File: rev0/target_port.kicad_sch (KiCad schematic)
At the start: 12 parts, among them IC1 ECP5-BGA256, U9 USB3343-CP

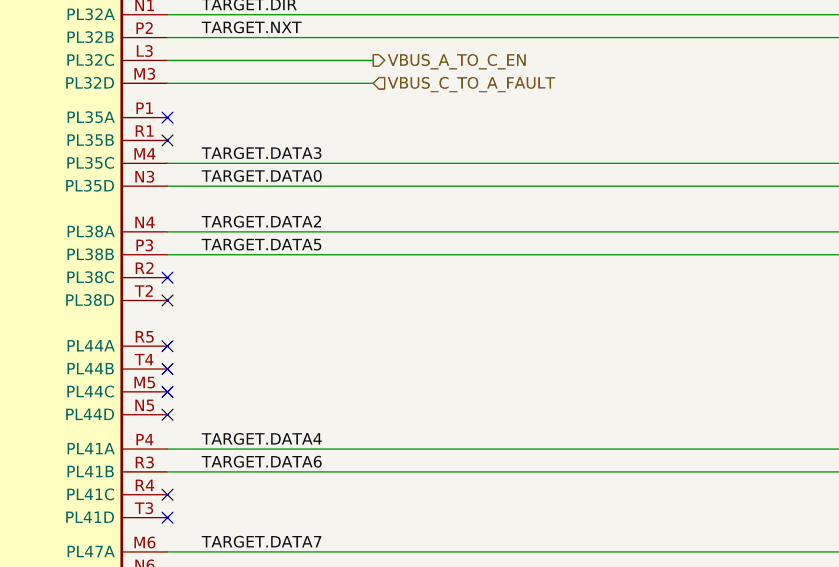
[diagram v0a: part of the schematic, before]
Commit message: hardware: add Target D+/D- full-speed monitor
allows FPGA to monitor low-speed or full-speed USB directly (instead of
or in addition to the high-speed PHY)
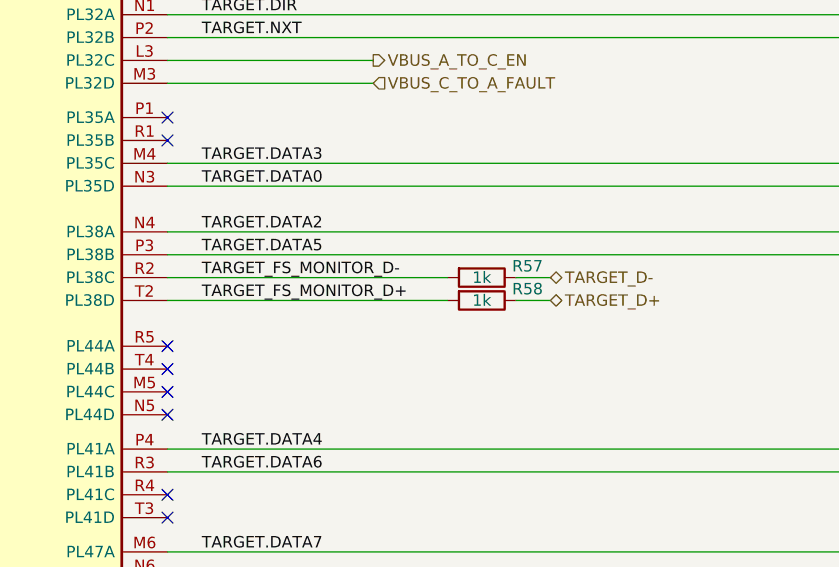
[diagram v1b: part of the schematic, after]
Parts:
- added R57, R58: 1k, Resistor_SMD:R_0402_1005Metric, symbol Device:R
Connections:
- net TARGET_D+: now also R58.1
- net TARGET_D-: now also R57.1
- net TARGET_FS_MONITOR_D-: now reaches IC1.R2 (PL38C)
- net TARGET_FS_MONITOR_D-: now also R57.2
- net TARGET_FS_MONITOR_D+: now reaches IC1.T2 (PL38D)
- net TARGET_FS_MONITOR_D+: now also R58.2
- no-connect marks 12 -> 10
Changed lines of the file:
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@@
   (junction (at 123.19 67.31) (diameter 0) (color 0 0 0 0)
   )
-  (no_connect (at 59.69 105.41))
-  (no_connect (at 59.69 107.95))
   (no_connect (at 59.69 118.11))
   (no_connect (at 59.69 115.57))
@@
     (stroke (width 0) (type default) (color 0 0 0 0))
   )
+  (wire (pts (xy 59.69 105.41) (xy 90.805 105.41))
+    (stroke (width 0) (type default) (color 0 0 0 0))
+  )
   (wire (pts (xy 59.69 72.39) (xy 137.16 72.39))
     (stroke (width 0) (type default) (color 0 0 0 0))
@@
     (stroke (width 0) (type default) (color 0 0 0 0))
   )
+  (wire (pts (xy 102.235 105.41) (xy 98.425 105.41))
+    (stroke (width 0) (type default) (color 0 0 0 0))
+  )
   (wire (pts (xy 231.14 63.5) (xy 226.06 63.5))
     (stroke (width 0) (type default) (color 0 0 0 0))
@@
     (stroke (width 0) (type default) (color 0 0 0 0))
   )
+  (wire (pts (xy 102.235 107.95) (xy 98.425 107.95))
+    (stroke (width 0) (type default) (color 0 0 0 0))
+  )
   (wire (pts (xy 165.1 90.17) (xy 190.5 90.17))
     (stroke (width 0) (type default) (color 0 0 0 0))
@@
     (stroke (width 0) (type default) (color 0 0 0 0))
   )
+  (wire (pts (xy 59.69 107.95) (xy 90.805 107.95))
+    (stroke (width 0) (type default) (color 0 0 0 0))
+  )
   (wire (pts (xy 41.91 31.75) (xy 41.91 34.29))
     (stroke (width 0) (type default) (color 0 0 0 0))
@@
     (effects (font (size 1.27 1.27)) (justify left bottom))
   )
+  (label "TARGET_FS_MONITOR_D-" (at 63.5 105.41 0)
+    (effects (font (size 1.27 1.27)) (justify left bottom))
+  )
   (label "TARGET.STP" (at 63.5 60.96 0)
     (effects (font (size 1.27 1.27)) (justify left bottom))
@@
   )
   (label "TARGET.NXT" (at 63.5 78.74 0)
+    (effects (font (size 1.27 1.27)) (justify left bottom))
+  )
+  (label "TARGET_FS_MONITOR_D+" (at 63.5 107.95 0)
     (effects (font (size 1.27 1.27)) (justify left bottom))
   )
@@
     (effects (font (size 1.27 1.27)) (justify left))
   )
+  (hierarchical_label "TARGET_D+" (shape bidirectional) (at 102.235 107.95 0)
+    (effects (font (size 1.27 1.27)) (justify left))
+  )
   (hierarchical_label "VBUS_C_TO_A_FAULT" (shape input) (at 82.55 83.82 0)
     (effects (font (size 1.27 1.27)) (justify left))
   )
   (hierarchical_label "VBUS_5V_TO_A_FAULT" (shape input) (at 82.55 55.88 0)
+    (effects (font (size 1.27 1.27)) (justify left))
+  )
+  (hierarchical_label "TARGET_D-" (shape bidirectional) (at 102.235 105.41 0)
     (effects (font (size 1.27 1.27)) (justify left))
   )
@@
     (pin "T9")
   )
+  (symbol (lib_id "Device:R") (at 94.615 105.41 270) (unit 1)
+    (in_bom yes) (on_board yes)
+    (property "Reference" "R57" (id 0) (at 99.695 104.14 90))
+    (property "Value" "1k" (id 1) (at 94.615 105.41 90))
+    (property "Footprint" "Resistor_SMD:R_0402_1005Metric" (id 2) (at 94.615 103.632 90)
+      (effects (font (size 1.27 1.27)) hide)
+    )
+    (property "Datasheet" "~" (id 3) (at 94.615 105.41 0)
+      (effects (font (size 1.27 1.27)) hide)
+    )
+    (property "Part Number" "GENERIC-RES-0402-1K" (id 4) (at 94.615 105.41 0)
+      (effects (font (size 1.27 1.27)) hide)
+    )
+    (property "Substitution" "any equivalent" (id 5) (at 94.615 105.41 0)
+      (effects (font (size 1.27 1.27)) hide)
+    )
+    (pin "1")
+    (pin "2")
+  )
+  (symbol (lib_id "Device:R") (at 94.615 107.95 270) (unit 1)
+    (in_bom yes) (on_board yes)
+    (property "Reference" "R58" (id 0) (at 99.695 106.68 90))
+    (property "Value" "1k" (id 1) (at 94.615 107.95 90))
+    (property "Footprint" "Resistor_SMD:R_0402_1005Metric" (id 2) (at 94.615 106.172 90)
+      (effects (font (size 1.27 1.27)) hide)
+    )
+    (property "Datasheet" "~" (id 3) (at 94.615 107.95 0)
+      (effects (font (size 1.27 1.27)) hide)
+    )
+    (property "Part Number" "GENERIC-RES-0402-1K" (id 4) (at 94.615 107.95 0)
+      (effects (font (size 1.27 1.27)) hide)
+    )
+    (property "Substitution" "any equivalent" (id 5) (at 94.615 107.95 0)
+      (effects (font (size 1.27 1.27)) hide)
+    )
+    (pin "1")
+    (pin "2")
+  )
 )

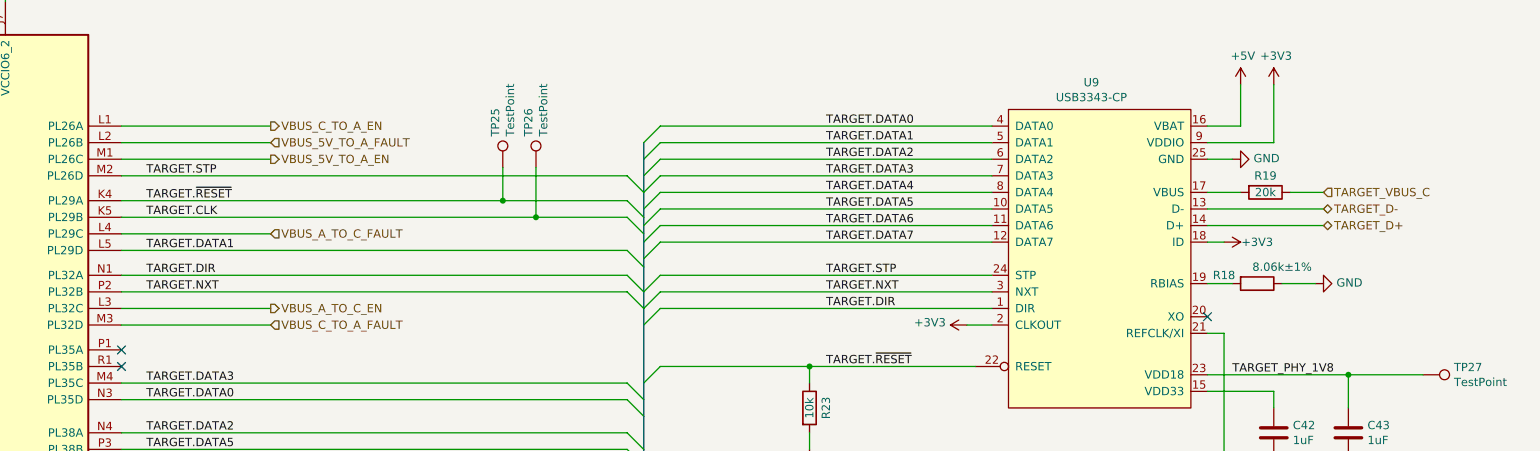
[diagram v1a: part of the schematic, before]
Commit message: hardware: replace VBUS pass-through switches
- increase maximum voltage with discrete FET solution
- pass through Control and Aux VBUS directly, not +5V supply rail
- add current sense resistors
- eliminate discharge current of previous power switches
- eliminate possible overvoltage condition of previous power switches
- remove 10 uF VBUS output capacitor C53
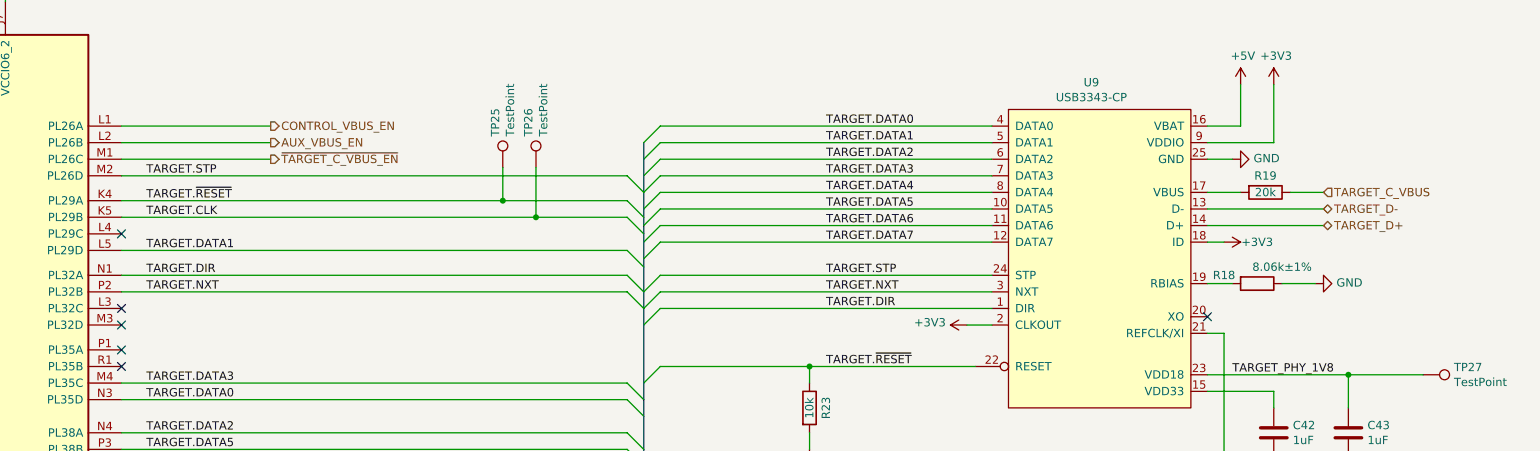
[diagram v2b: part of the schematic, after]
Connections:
- net TARGET_VBUS_C renamed TARGET_C_VBUS
- net VBUS_5V_TO_A_EN renamed ~{TARGET_C_VBUS_EN}
- net VBUS_5V_TO_A_FAULT renamed AUX_VBUS_EN
- net VBUS_A_TO_C_EN: no longer names the net of IC1.L3 (PL32C)
- net VBUS_A_TO_C_FAULT: no longer names the net of IC1.L4 (PL29C)
- net VBUS_C_TO_A_EN renamed CONTROL_VBUS_EN
- net VBUS_C_TO_A_FAULT: no longer names the net of IC1.M3 (PL32D)
- no-connect marks 10 -> 13
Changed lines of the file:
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@@
   (title_block
     (title "LUNA USB Multitool")
-    (date "2023-02-07")
+    (date "2023-02-16")
     (rev "r0.5+")
     (company "Copyright 2019-2023 Great Scott Gadgets")
@@
   (junction (at 123.19 67.31) (diameter 0) (color 0 0 0 0)
   )
+  (no_connect (at 59.69 83.82))
   (no_connect (at 59.69 118.11))
+  (no_connect (at 59.69 81.28))
   (no_connect (at 59.69 115.57))
   (no_connect (at 59.69 87.63))
   (no_connect (at 226.06 82.55))
+  (no_connect (at 59.69 69.85))
   (no_connect (at 59.69 120.65))
   (no_connect (at 59.69 143.51))
@@
     (stroke (width 0) (type default) (color 0 0 0 0))
   )
-  (wire (pts (xy 59.69 81.28) (xy 82.55 81.28))
-    (stroke (width 0) (type default) (color 0 0 0 0))
-  )
   (bus (pts (xy 139.7 55.88) (xy 139.7 58.42))
     (stroke (width 0) (type default) (color 0 0 0 0))
@@
     (stroke (width 0) (type default) (color 0 0 0 0))
   )
-  (wire (pts (xy 82.55 69.85) (xy 59.69 69.85))
-    (stroke (width 0) (type default) (color 0 0 0 0))
-  )
   (wire (pts (xy 59.69 78.74) (xy 137.16 78.74))
     (stroke (width 0) (type default) (color 0 0 0 0))
@@
     (stroke (width 0) (type default) (color 0 0 0 0))
   )
-  (wire (pts (xy 82.55 83.82) (xy 59.69 83.82))
-    (stroke (width 0) (type default) (color 0 0 0 0))
-  )
   (bus (pts (xy 139.7 95.25) (xy 139.7 97.79))
     (stroke (width 0) (type default) (color 0 0 0 0))
@@
     (effects (font (size 1.27 1.27)) (justify left bottom))
   )
-  (hierarchical_label "VBUS_A_TO_C_EN" (shape output) (at 82.55 81.28 0)
+  (hierarchical_label "CONTROL_VBUS_EN" (shape output) (at 82.55 53.34 0)
     (effects (font (size 1.27 1.27)) (justify left))
   )
@@
     (effects (font (size 1.27 1.27)) (justify left))
   )
-  (hierarchical_label "TARGET_VBUS_C" (shape input) (at 243.84 63.5 0)
+  (hierarchical_label "~{TARGET_C_VBUS_EN}" (shape output) (at 82.55 58.42 0)
+    (effects (font (size 1.27 1.27)) (justify left))
+  )
+  (hierarchical_label "TARGET_C_VBUS" (shape input) (at 243.84 63.5 0)
     (effects (font (size 1.27 1.27)) (justify left))
   )
@@
     (effects (font (size 1.27 1.27)) (justify left))
   )
-  (hierarchical_label "VBUS_A_TO_C_FAULT" (shape input) (at 82.55 69.85 0)
-    (effects (font (size 1.27 1.27)) (justify left))
-  )
-  (hierarchical_label "VBUS_C_TO_A_EN" (shape output) (at 82.55 53.34 0)
-    (effects (font (size 1.27 1.27)) (justify left))
-  )
-  (hierarchical_label "VBUS_5V_TO_A_EN" (shape output) (at 82.55 58.42 0)
+  (hierarchical_label "AUX_VBUS_EN" (shape output) (at 82.55 55.88 0)
     (effects (font (size 1.27 1.27)) (justify left))
   )
@@
     (effects (font (size 1.27 1.27)) (justify left))
   )
-  (hierarchical_label "VBUS_C_TO_A_FAULT" (shape input) (at 82.55 83.82 0)
-    (effects (font (size 1.27 1.27)) (justify left))
-  )
-  (hierarchical_label "VBUS_5V_TO_A_FAULT" (shape input) (at 82.55 55.88 0)
-    (effects (font (size 1.27 1.27)) (justify left))
-  )

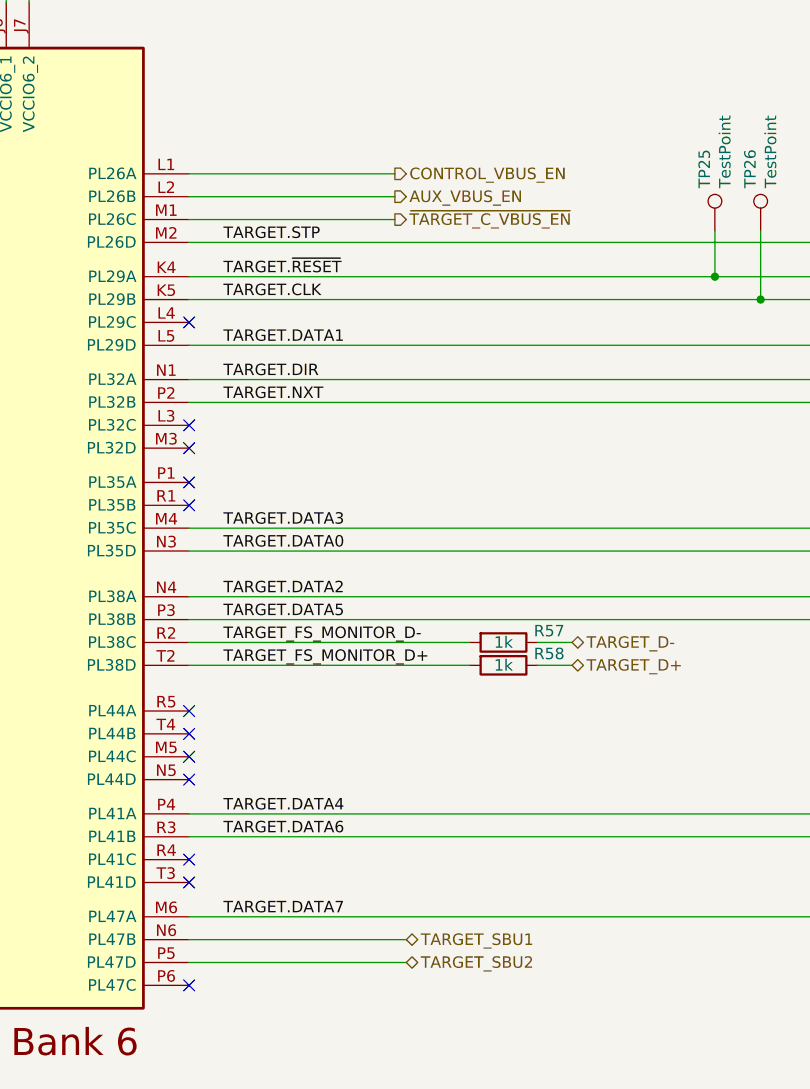
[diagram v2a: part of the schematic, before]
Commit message: hardware: add VBUS voltage and current monitoring
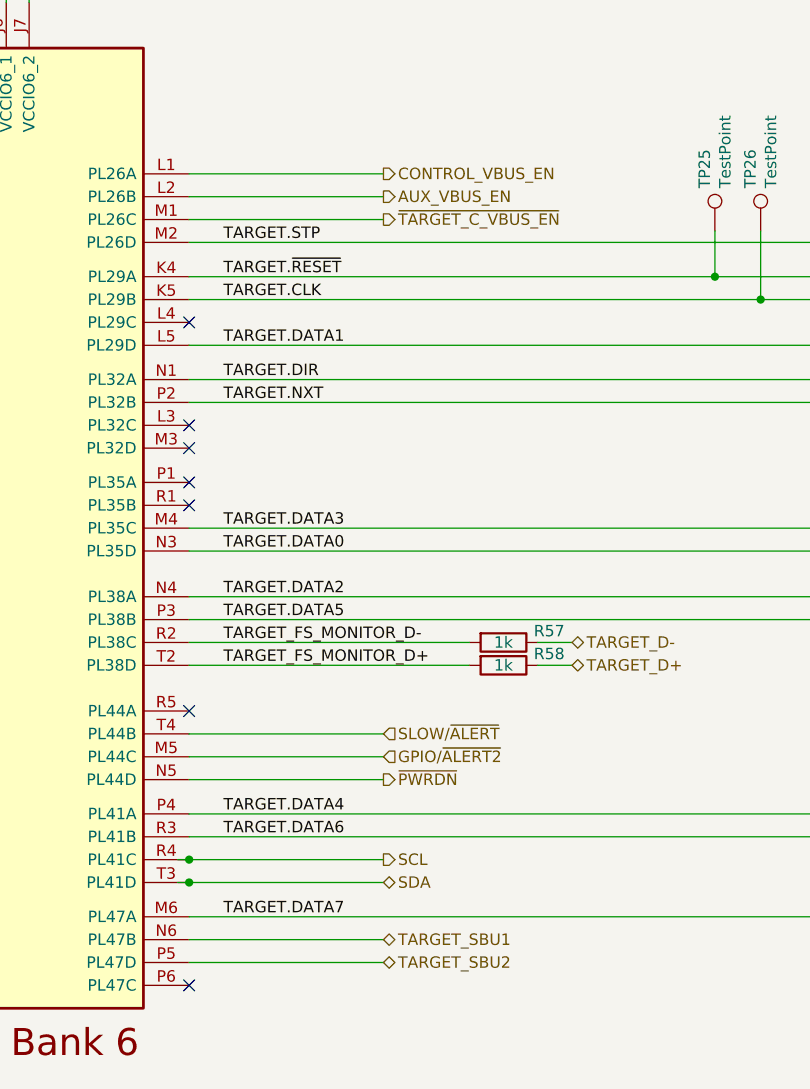
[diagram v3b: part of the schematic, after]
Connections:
- net GPIO/~{ALERT2}: now reaches IC1.M5 (PL44C)
- net ~{PWRDN}: now reaches IC1.N5 (PL44D)
- net SCL: now reaches IC1.R4 (PL41C)
- net SDA: now reaches IC1.T3 (PL41D)
- net SLOW/~{ALERT}: now reaches IC1.T4 (PL44B)
- no-connect marks 13 -> 8
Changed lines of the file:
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@@
   (junction (at 165.1 90.17) (diameter 0) (color 0 0 0 0)
   )
+  (junction (at 59.69 129.54) (diameter 0) (color 0 0 0 0)
+  )
   (junction (at 118.11 64.77) (diameter 0) (color 0 0 0 0)
   )
   (junction (at 247.65 91.44) (diameter 0) (color 0 0 0 0)
   )
+  (junction (at 59.69 132.08) (diameter 0) (color 0 0 0 0)
+  )
   (junction (at 123.19 67.31) (diameter 0) (color 0 0 0 0)
   )
   (no_connect (at 59.69 83.82))
-  (no_connect (at 59.69 118.11))
   (no_connect (at 59.69 81.28))
-  (no_connect (at 59.69 115.57))
   (no_connect (at 59.69 87.63))
   (no_connect (at 226.06 82.55))
   (no_connect (at 59.69 69.85))
-  (no_connect (at 59.69 120.65))
   (no_connect (at 59.69 143.51))
-  (no_connect (at 59.69 129.54))
   (no_connect (at 59.69 90.17))
-  (no_connect (at 59.69 132.08))
   (no_connect (at 59.69 113.03))
   (bus_entry (at 139.7 83.82) (size 2.54 -2.54)
@@
     (stroke (width 0) (type default) (color 0 0 0 0))
   )
+  (wire (pts (xy 81.28 129.54) (xy 59.69 129.54))
+    (stroke (width 0) (type default) (color 0 0 0 0))
+  )
   (wire (pts (xy 193.04 63.5) (xy 142.24 63.5))
     (stroke (width 0) (type default) (color 0 0 0 0))
@@
     (stroke (width 0) (type default) (color 0 0 0 0))
   )
+  (wire (pts (xy 58.42 132.08) (xy 59.69 132.08))
+    (stroke (width 0) (type default) (color 0 0 0 0))
+  )
   (wire (pts (xy 217.17 130.81) (xy 217.17 133.35))
     (stroke (width 0) (type default) (color 0 0 0 0))
@@
     (stroke (width 0) (type default) (color 0 0 0 0))
   )
-  (wire (pts (xy 82.55 58.42) (xy 59.69 58.42))
+  (wire (pts (xy 81.28 58.42) (xy 59.69 58.42))
     (stroke (width 0) (type default) (color 0 0 0 0))
   )
@@
     (stroke (width 0) (type default) (color 0 0 0 0))
   )
-  (wire (pts (xy 59.69 55.88) (xy 82.55 55.88))
+  (wire (pts (xy 59.69 55.88) (xy 81.28 55.88))
     (stroke (width 0) (type default) (color 0 0 0 0))
   )
@@
     (stroke (width 0) (type default) (color 0 0 0 0))
   )
+  (wire (pts (xy 81.28 118.11) (xy 59.69 118.11))
+    (stroke (width 0) (type default) (color 0 0 0 0))
+  )
   (wire (pts (xy 236.22 55.88) (xy 226.06 55.88))
     (stroke (width 0) (type default) (color 0 0 0 0))
@@
     (stroke (width 0) (type default) (color 0 0 0 0))
   )
-  (wire (pts (xy 83.82 140.97) (xy 59.69 140.97))
+  (wire (pts (xy 81.28 140.97) (xy 59.69 140.97))
     (stroke (width 0) (type default) (color 0 0 0 0))
   )
@@
     (stroke (width 0) (type default) (color 0 0 0 0))
   )
+  (wire (pts (xy 59.69 132.08) (xy 81.28 132.08))
+    (stroke (width 0) (type default) (color 0 0 0 0))
+  )
   (wire (pts (xy 59.69 100.33) (xy 137.16 100.33))
     (stroke (width 0) (type default) (color 0 0 0 0))
@@
     (stroke (width 0) (type default) (color 0 0 0 0))
   )
+  (wire (pts (xy 59.69 120.65) (xy 81.28 120.65))
+    (stroke (width 0) (type default) (color 0 0 0 0))
+  )
   (wire (pts (xy 193.04 68.58) (xy 142.24 68.58))
     (stroke (width 0) (type default) (color 0 0 0 0))
   )
-  (wire (pts (xy 59.69 53.34) (xy 82.55 53.34))
+  (wire (pts (xy 59.69 53.34) (xy 81.28 53.34))
     (stroke (width 0) (type default) (color 0 0 0 0))
   )
@@
     (stroke (width 0) (type default) (color 0 0 0 0))
   )
+  (wire (pts (xy 58.42 129.54) (xy 59.69 129.54))
+    (stroke (width 0) (type default) (color 0 0 0 0))
+  )
   (wire (pts (xy 39.37 34.29) (xy 39.37 31.75))
     (stroke (width 0) (type default) (color 0 0 0 0))
@@
     (stroke (width 0) (type default) (color 0 0 0 0))
   )
-  (wire (pts (xy 83.82 138.43) (xy 59.69 138.43))
+  (wire (pts (xy 81.28 138.43) (xy 59.69 138.43))
+    (stroke (width 0) (type default) (color 0 0 0 0))
+  )
+  (wire (pts (xy 59.69 115.57) (xy 81.28 115.57))
     (stroke (width 0) (type default) (color 0 0 0 0))
   )
@@
     (effects (font (size 1.27 1.27)) (justify left bottom))
   )
-  (hierarchical_label "CONTROL_VBUS_EN" (shape output) (at 82.55 53.34 0)
+  (hierarchical_label "CONTROL_VBUS_EN" (shape output) (at 81.28 53.34 0)
+    (effects (font (size 1.27 1.27)) (justify left))
+  )
+  (hierarchical_label "SLOW{slash}~{ALERT}" (shape input) (at 81.28 115.57 0)
     (effects (font (size 1.27 1.27)) (justify left))
   )
@@
     (effects (font (size 1.27 1.27)) (justify left))
   )
-  (hierarchical_label "TARGET_SBU2" (shape bidirectional) (at 83.82 140.97 0)
-    (effects (font (size 1.27 1.27)) (justify left))
-  )
-  (hierarchical_label "~{TARGET_C_VBUS_EN}" (shape output) (at 82.55 58.42 0)
+  (hierarchical_label "TARGET_SBU2" (shape bidirectional) (at 81.28 140.97 0)
+    (effects (font (size 1.27 1.27)) (justify left))
+  )
+  (hierarchical_label "~{TARGET_C_VBUS_EN}" (shape output) (at 81.28 58.42 0)
     (effects (font (size 1.27 1.27)) (justify left))
   )
@@
     (effects (font (size 1.27 1.27)) (justify left))
   )
-  (hierarchical_label "TARGET_SBU1" (shape bidirectional) (at 83.82 138.43 0)
-    (effects (font (size 1.27 1.27)) (justify left))
-  )
-  (hierarchical_label "AUX_VBUS_EN" (shape output) (at 82.55 55.88 0)
+  (hierarchical_label "TARGET_SBU1" (shape bidirectional) (at 81.28 138.43 0)
+    (effects (font (size 1.27 1.27)) (justify left))
+  )
+  (hierarchical_label "GPIO{slash}~{ALERT2}" (shape input) (at 81.28 118.11 0)
+    (effects (font (size 1.27 1.27)) (justify left))
+  )
+  (hierarchical_label "AUX_VBUS_EN" (shape output) (at 81.28 55.88 0)
+    (effects (font (size 1.27 1.27)) (justify left))
+  )
+  (hierarchical_label "SDA" (shape bidirectional) (at 81.28 132.08 0)
+    (effects (font (size 1.27 1.27)) (justify left))
+  )
+  (hierarchical_label "SCL" (shape output) (at 81.28 129.54 0)
     (effects (font (size 1.27 1.27)) (justify left))
   )
@@
     (effects (font (size 1.27 1.27)) (justify left))
   )
+  (hierarchical_label "~{PWRDN}" (shape output) (at 81.28 120.65 0)
+    (effects (font (size 1.27 1.27)) (justify left))
+  )
